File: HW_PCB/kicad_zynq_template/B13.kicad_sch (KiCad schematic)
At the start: 8 parts, among them U2 XA7Z020-1CLG400I

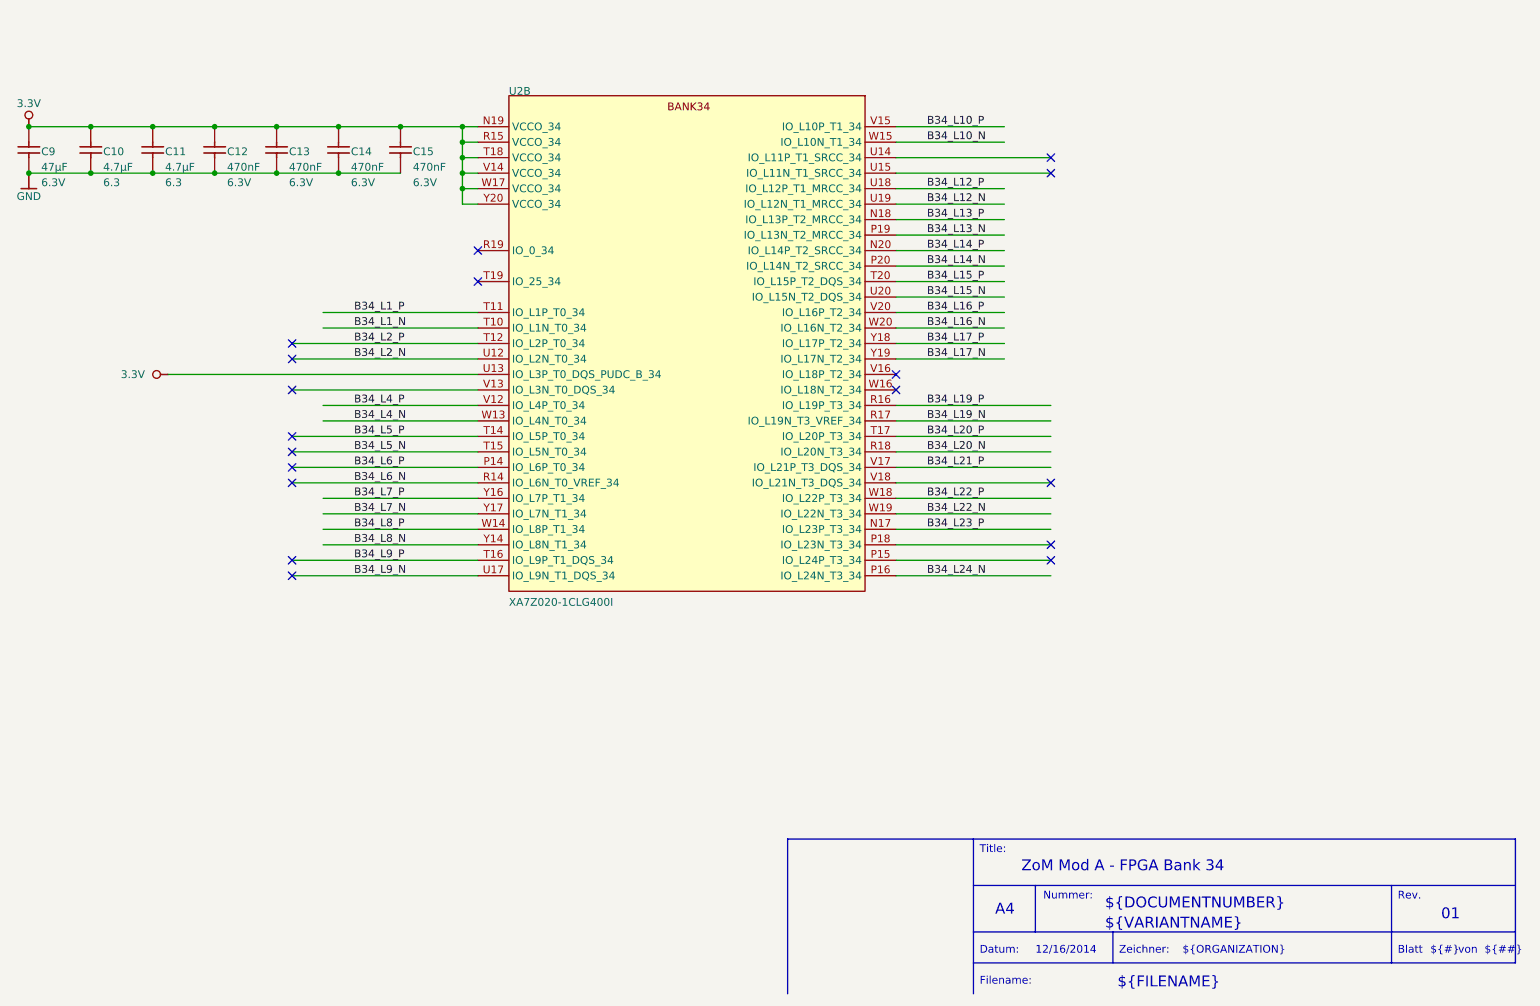
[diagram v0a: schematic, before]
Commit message: pcbs tidied up
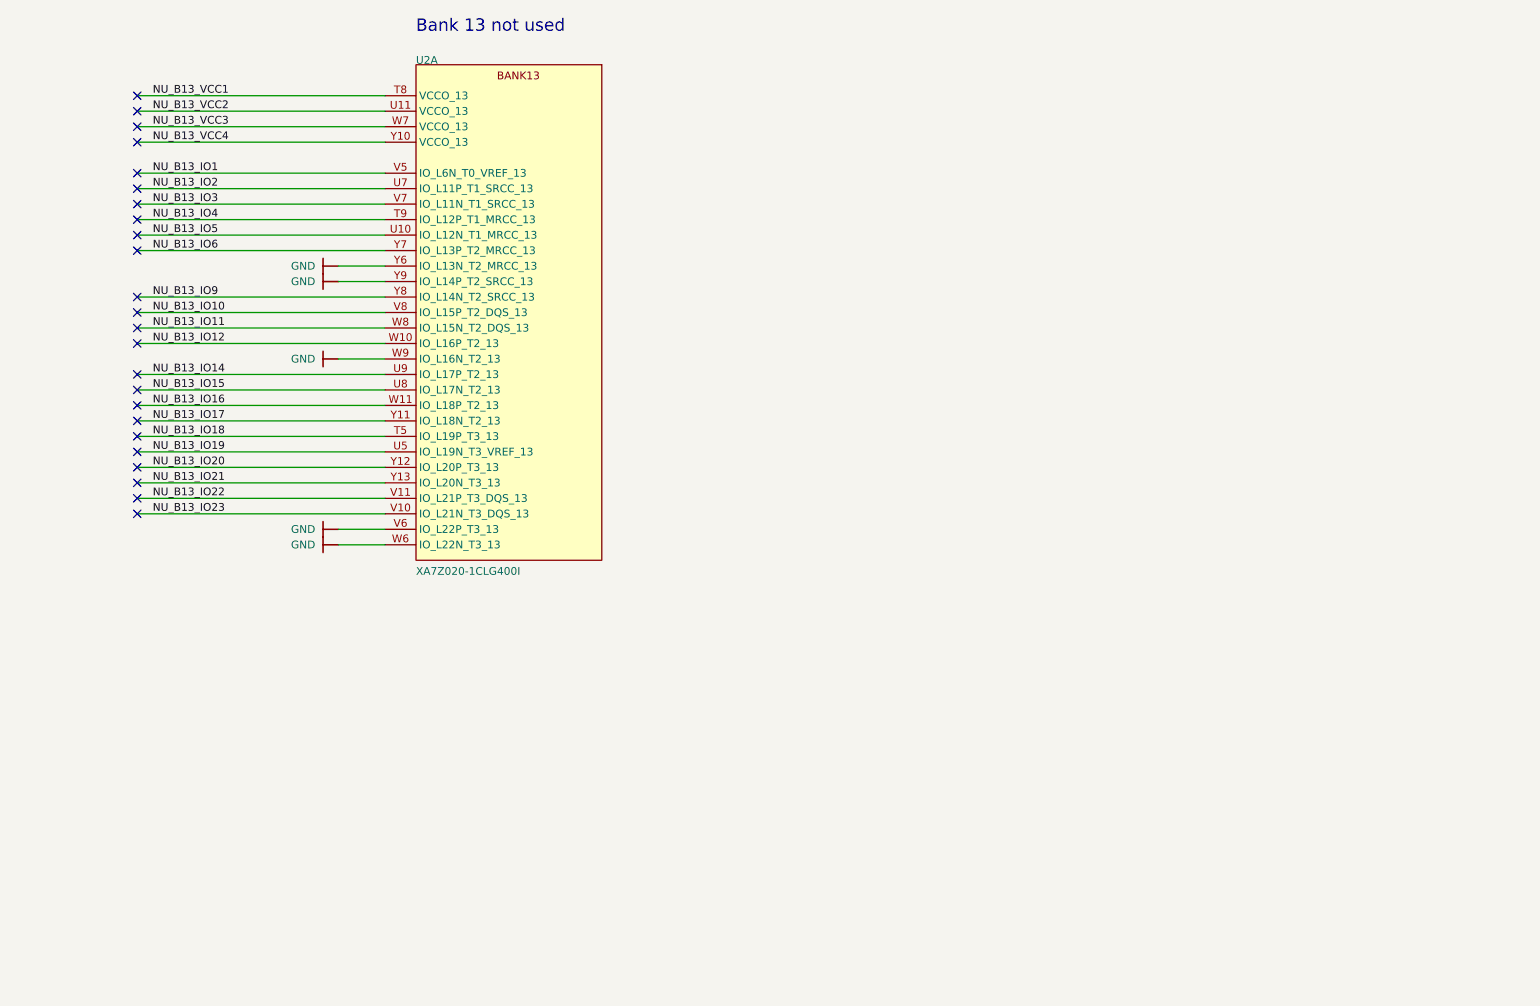
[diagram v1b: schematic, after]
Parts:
- removed C10, C11: 4.7µF, CAPC1005X60N, symbol TE0719-altium-import:B34_0_CAP-NP
- removed C12, C13, C14, C15: 470nF, CAPC0603X33N, symbol TE0719-altium-import:B34_0_CAP-NP
- removed C9: 47µF, CAPC3216X180N, symbol TE0719-altium-import:B34_0_CAP-NP
- removed U2: XA7Z020-1CLG400I, BGA400C80P20X20_1700X1700X160N, symbol TE0719-altium-import:B34_0_XC7Z020-2CLG400C
- added U2: XA7Z020-1CLG400I, BGA400C80P20X20_1700X1700X160N, symbol TE0719-altium-import:B13_0_XC7Z020-2CLG400C
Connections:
- net GND: now also U2.V6 (IO_L22P_T3_13), U2.W6 (IO_L22N_T3_13), U2.W9 (IO_L16N_T2_13), U2.Y6 (IO_L13N_T2_MRCC_13), U2.Y9 (IO_L14P_T2_SRCC_13)
- new net NU_B13_IO1: U2.V5 (IO_L6N_T0_VREF_13)
- new net NU_B13_IO10: U2.V8 (IO_L15P_T2_DQS_13)
- new net NU_B13_IO11: U2.W8 (IO_L15N_T2_DQS_13)
- new net NU_B13_IO12: U2.W10 (IO_L16P_T2_13)
- new net NU_B13_IO14: U2.U9 (IO_L17P_T2_13)
- new net NU_B13_IO15: U2.U8 (IO_L17N_T2_13)
- new net NU_B13_IO16: U2.W11 (IO_L18P_T2_13)
- new net NU_B13_IO17: U2.Y11 (IO_L18N_T2_13)
- new net NU_B13_IO18: U2.T5 (IO_L19P_T3_13)
- new net NU_B13_IO19: U2.U5 (IO_L19N_T3_VREF_13)
- new net NU_B13_IO2: U2.U7 (IO_L11P_T1_SRCC_13)
- new net NU_B13_IO20: U2.Y12 (IO_L20P_T3_13)
- new net NU_B13_IO21: U2.Y13 (IO_L20N_T3_13)
- new net NU_B13_IO22: U2.V11 (IO_L21P_T3_DQS_13)
- new net NU_B13_IO23: U2.V10 (IO_L21N_T3_DQS_13)
- new net NU_B13_IO3: U2.V7 (IO_L11N_T1_SRCC_13)
- new net NU_B13_IO4: U2.T9 (IO_L12P_T1_MRCC_13)
- new net NU_B13_IO5: U2.U10 (IO_L12N_T1_MRCC_13)
- new net NU_B13_IO6: U2.Y7 (IO_L13P_T2_MRCC_13)
- new net NU_B13_IO9: U2.Y8 (IO_L14N_T2_SRCC_13)
- new net NU_B13_VCC1: U2.T8 (VCCO_13)
- new net NU_B13_VCC2: U2.U11 (VCCO_13)
- new net NU_B13_VCC3: U2.W7 (VCCO_13)
- new net NU_B13_VCC4: U2.Y10 (VCCO_13)
- no-connect marks 18 -> 24
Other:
- note added: "Bank 13 not used"
- note removed: "${##}"
- note removed: "${#}"
- note removed: "${DOCUMENTNUMBER}"
- note removed: "${FILENAME}"
- note removed: "${ISSUE_DATE}"
- note removed: "${ORGANIZATION}"
- note removed: "${REVISION}"
- note removed: "${TITLE}"
- note removed: "${VARIANTNAME}"
- note removed: "A4"
- note removed: "Blatt"
- note removed: "Datum:"
- note removed: "Filename:"
- note removed: "Nummer:"
- note removed: "Rev."
- note removed: "Title:"
- note removed: "Zeichner:"
- note removed: "von"
- title: ZoM Mod A - FPGA Bank 34 -> ZoM Mod A - FPGA Bank 13
